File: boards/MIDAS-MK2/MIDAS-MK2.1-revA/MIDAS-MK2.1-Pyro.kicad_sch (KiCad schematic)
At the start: 46 parts, among them J201 Conn_01x02, Q202 DMNH6022SSDQ, Q203 DMNH6022SSDQ, U1 TCAL9539-Q1, U2 ISOW7742, U3 ISO1640BDR, U4 ADS122C04IRTE, U5 INA745x

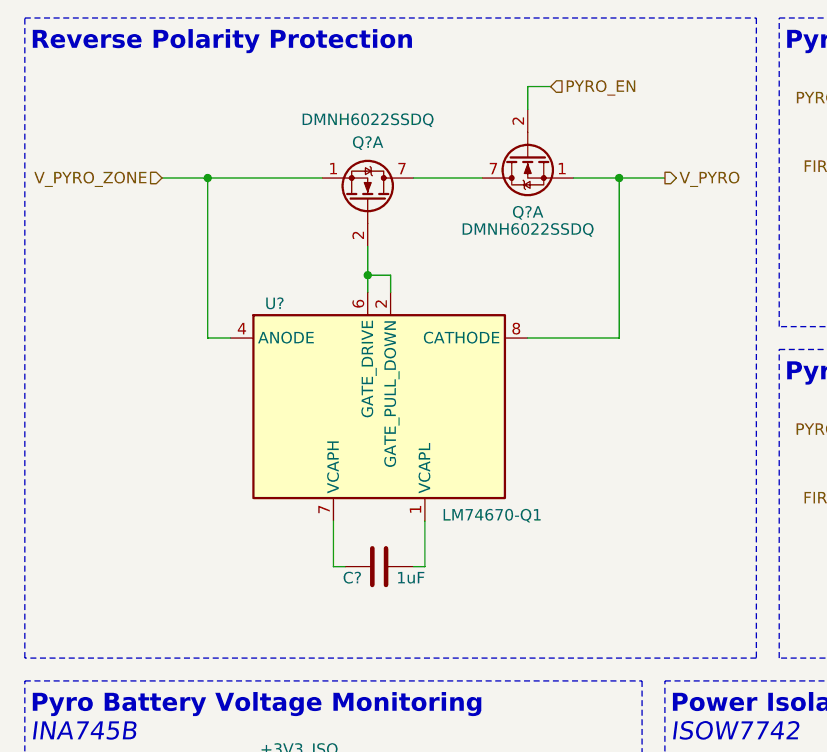
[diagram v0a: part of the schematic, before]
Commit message: changed pyro reverse polarity protection to diode
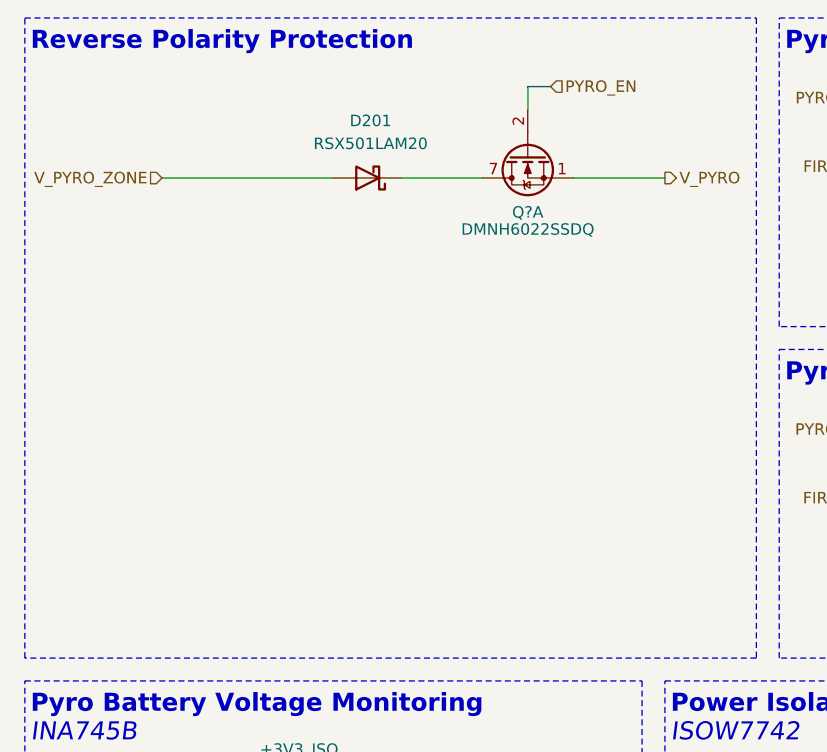
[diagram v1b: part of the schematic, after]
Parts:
- removed C?: 1uF, Capacitor_SMD:C_0603_1608Metric, symbol Device:C
- removed Q?: DMNH6022SSDQ, Package_SO:SO-8_3.9x4.9mm_P1.27mm, symbol Transistor_FET_Diodes:DMNH6022SSDQ
- removed U?: LM74670-Q1, Package_SO:VSSOP-8_3x3mm_P0.65mm, symbol Power_Ideal_Diode:LM74670-Q1
- added D201: RSX501LAM20, Diode_SMD:D_SOD-128, symbol Device:D_Schottky
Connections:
- net V_PYRO_ZONE: now also D201.2 (A)
- net at Q?.7 (D1), Q?.8 (D1): now also D201.1 (K)

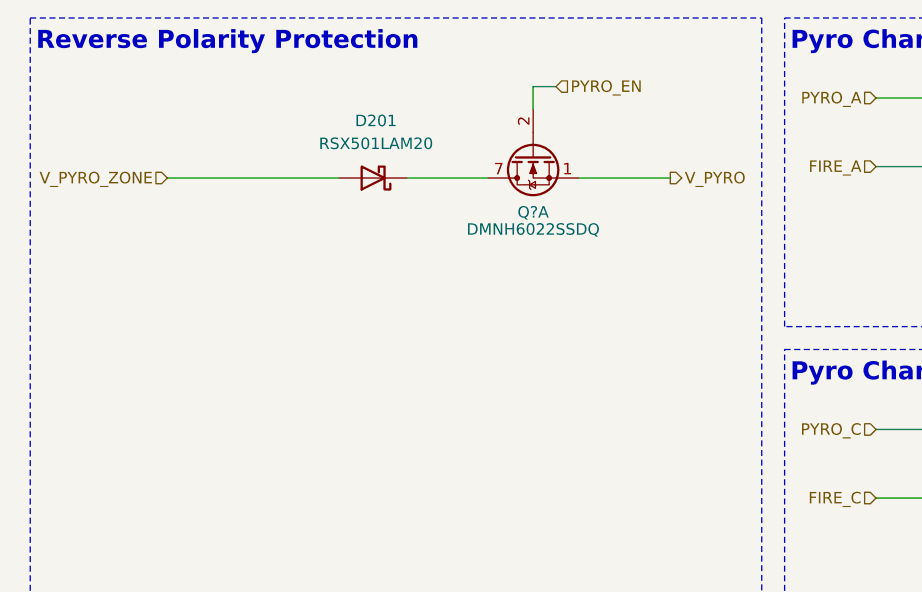
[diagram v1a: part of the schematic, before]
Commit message: Replaced high-side pyro switch
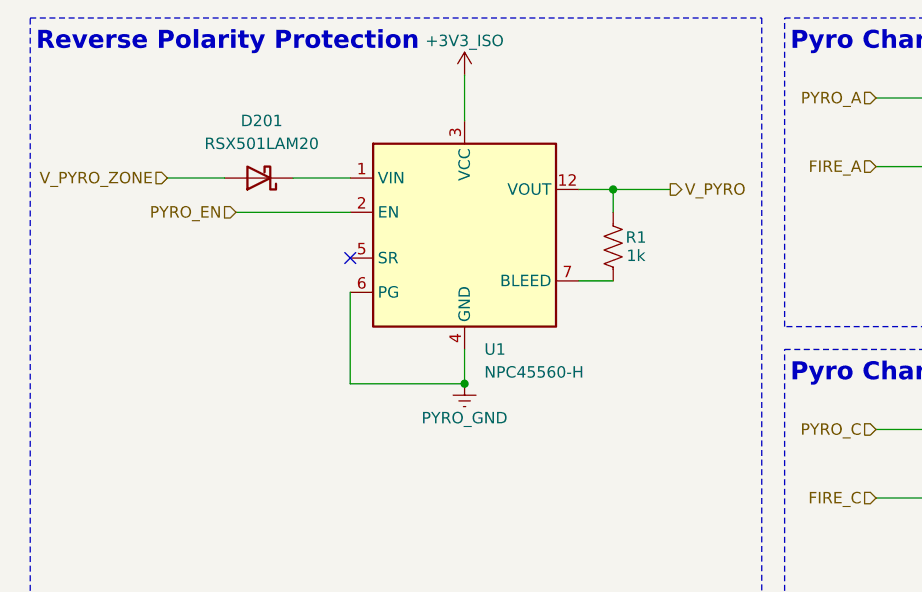
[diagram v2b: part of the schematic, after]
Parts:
- removed Q?: DMNH6022SSDQ, Package_SO:SO-8_3.9x4.9mm_P1.27mm, symbol Transistor_FET_Diodes:DMNH6022SSDQ
- added R1: 1k, Resistor_SMD:R_0603_1608Metric, symbol Device:R_US
- added U1: NPC45560-H, Package_DFN_QFN:DFN-12-1EP_3x3mm_P0.5mm_EP2.05x2.86mm, symbol Power_Management:NPC45560-H
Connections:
- net +3V3_ISO: now also U1.3 (VCC)
- net PYRO_EN: now also U1.2 (EN)
- net PYRO_GND: now also U1.4 (GND), U1.6 (PG)
- net V_PYRO: now also R1.1, U1.10 (VOUT), U1.11 (VOUT), U1.12 (VOUT), U1.8 (VOUT), U1.9 (VOUT)
- net at D201.1 (K): now also U1.1 (VIN), U1.13 (VIN)
- new net: R1.2, U1.7 (BLEED)
- no-connect marks 11 -> 12
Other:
- moved on the sheet: D201

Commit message: pyro formatting changes
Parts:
- added R220, R222: 4.7k, Resistor_SMD:R_0603_1608Metric, symbol Device:R_US
- added R223: 10k, Resistor_SMD:R_0603_1608Metric, symbol Device:R_US
- renumbered C211 to C210, C212 to C211, C213 to C212, Q202 to Q201, Q203 to Q202, R1 to R202, R202 to R203, R220 to R224, U1 to U202
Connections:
- net +3V3_ISO: now also R220.2, R222.2, R223.2
- net ADC_DRDY: now also U1.8 (P07); no longer U1.7 (P06)
- net ADC_RST_ISO: now also U1.7 (P06), R223.1
- net ISO_SCL: now also R222.1
- net ISO_SDA: now also R220.1
- no-connect marks 12 -> 11
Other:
- note added: "Global Enable & Reverse Polarity Protection"
- note added: "Pull-Up Resistors"
- note removed: "Reverse Polarity Protection"
- moved on the sheet: D201, J201, R202, U202

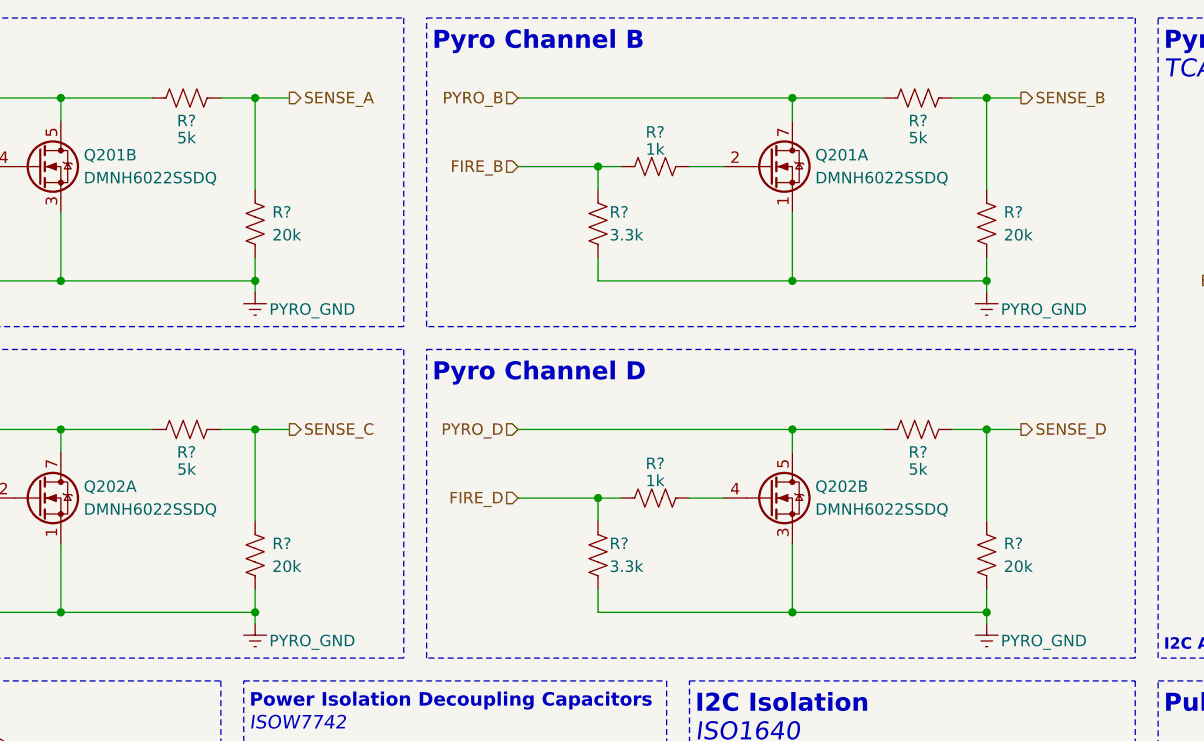
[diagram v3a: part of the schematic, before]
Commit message: updated pyro voltage dividers
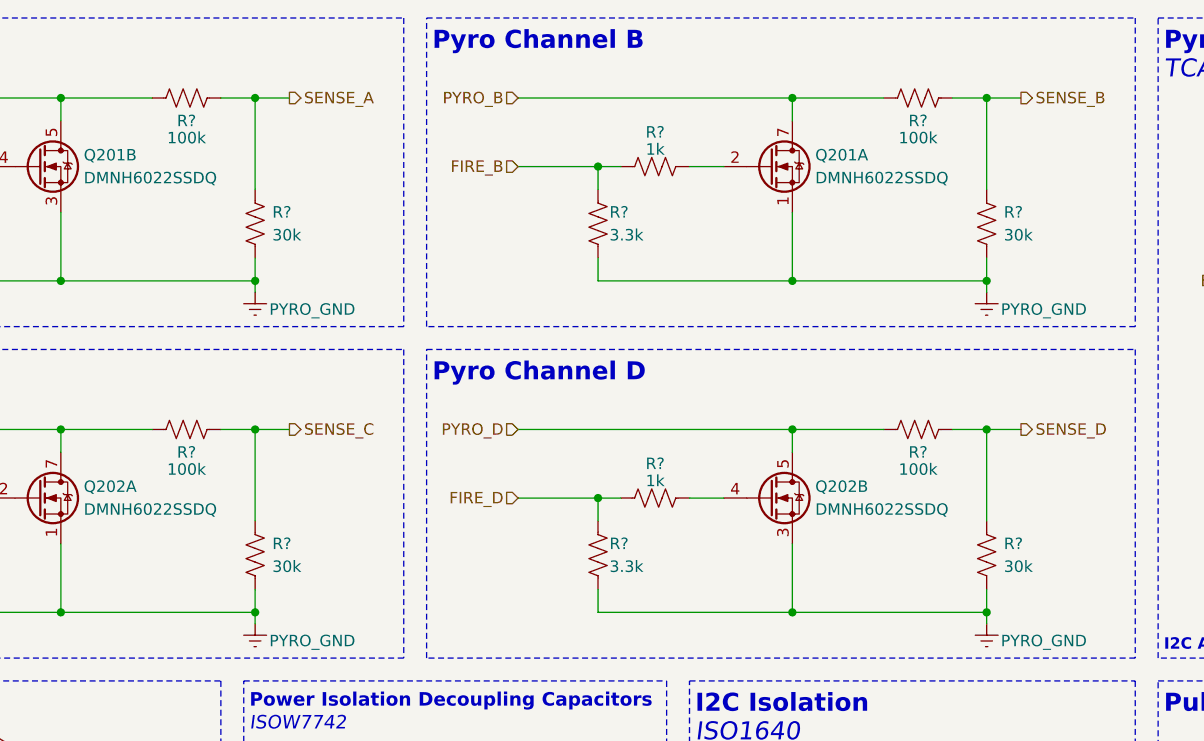
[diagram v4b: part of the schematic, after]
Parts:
- R? (x4): value 20k -> 30k
- R? (x4): value 5k -> 100k
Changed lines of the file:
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@@
 			)
 		)
-		(property "Value" "20k"
+		(property "Value" "30k"
 			(at 244.475 76.2 0)
 			(effects
@@
 			)
 		)
-		(property "Value" "5k"
+		(property "Value" "100k"
 			(at 153.67 65.405 90)
 			(effects
@@
 			)
 		)
-		(property "Value" "5k"
+		(property "Value" "100k"
 			(at 153.67 28.575 90)
 			(effects
@@
 			)
 		)
-		(property "Value" "20k"
+		(property "Value" "30k"
 			(at 244.475 39.37 0)
 			(effects
@@
 			)
 		)
-		(property "Value" "5k"
+		(property "Value" "100k"
 			(at 234.95 28.575 90)
 			(effects
@@
 			)
 		)
-		(property "Value" "20k"
+		(property "Value" "30k"
 			(at 163.195 39.37 0)
 			(effects
@@
 			)
 		)
-		(property "Value" "20k"
+		(property "Value" "30k"
 			(at 163.195 76.2 0)
 			(effects
@@
 			)
 		)
-		(property "Value" "5k"
+		(property "Value" "100k"
 			(at 234.95 65.405 90)
 			(effects

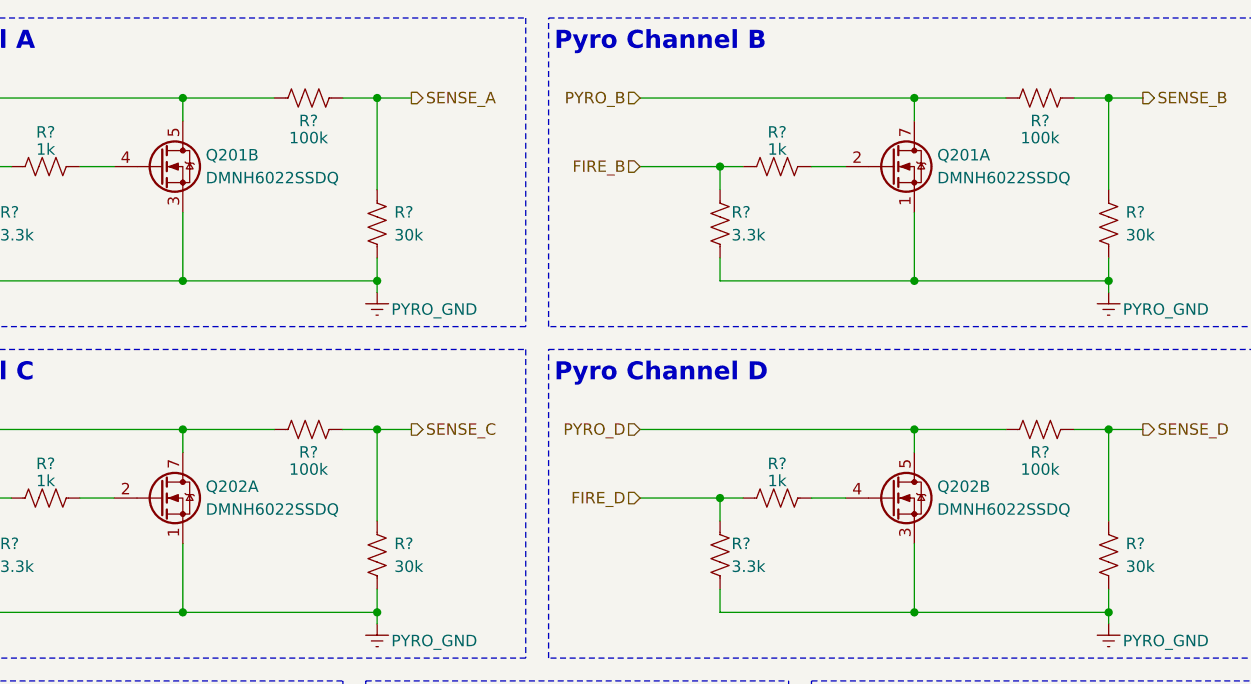
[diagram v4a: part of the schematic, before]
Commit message: switched from DMNH6022SSDQ to Si7232DN
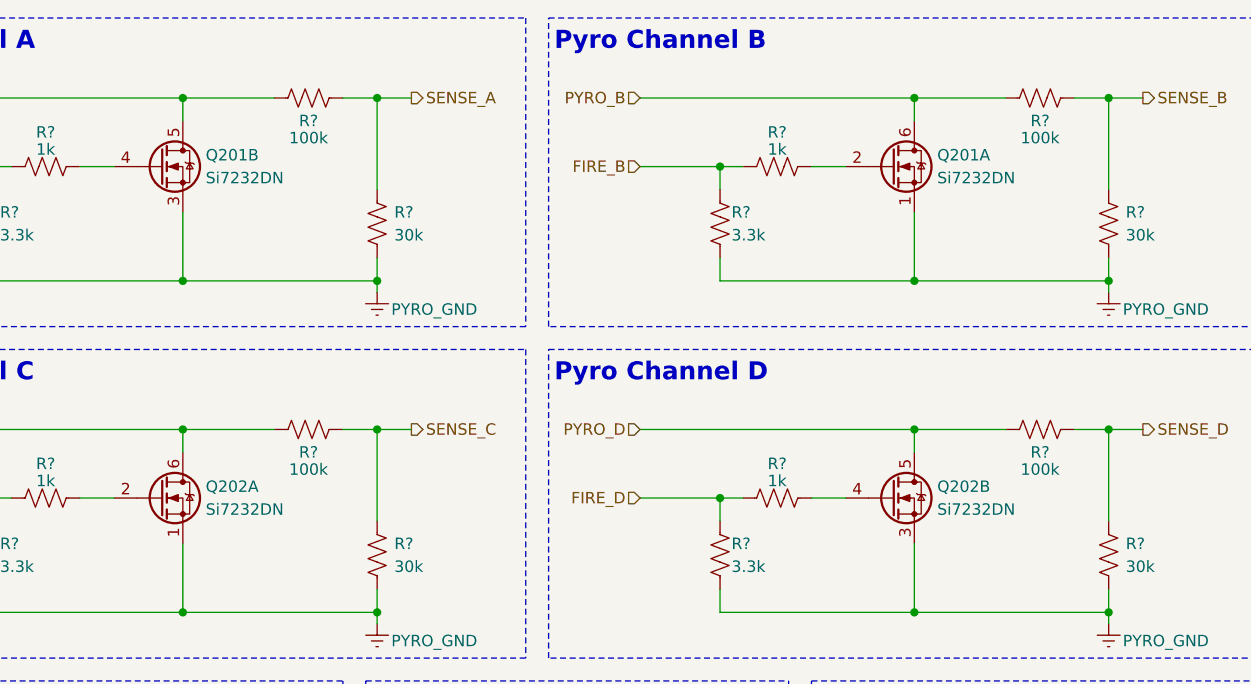
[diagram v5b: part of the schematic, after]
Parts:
- removed Q201, Q202: DMNH6022SSDQ, Package_SO:SO-8_3.9x4.9mm_P1.27mm, symbol Transistor_FET_Diodes:DMNH6022SSDQ
- added Q201, Q202: Si7232DN, Transistor_FET_Vishay:Vishay_PowerPAK_1212-8_Dual, symbol Transistor_FET_Vishay:Si7232DN
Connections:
- net PYRO_A: now also Q201.5 (D2)
- net PYRO_B: now also Q201.6 (D1)
- net PYRO_C: now also Q202.6 (D1)
- net PYRO_D: now also Q202.5 (D2)
- net PYRO_GND: now also Q201.1 (S1), Q201.3 (S2), Q202.1 (S1), Q202.3 (S2)
- net at R?.2: now also Q202.4 (G2)
- net at R?.2: now also Q201.2 (G1)
- net at R?.2: now also Q202.2 (G1)
- net at R?.2: now also Q201.4 (G2)
